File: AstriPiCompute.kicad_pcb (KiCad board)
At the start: 2 copper layers, 50.8 x 74.9 mm, 37 parts, among them J01_OUT1 12V, J02_OUT1 12V, J03_OUT1 12V, J1 Connector-ML_RPi_GPIO, Q1 TIP3055, Q2 TIP122, Q3 TIP122, U1 IRF7313, U2 MP1584EN-LF-Z

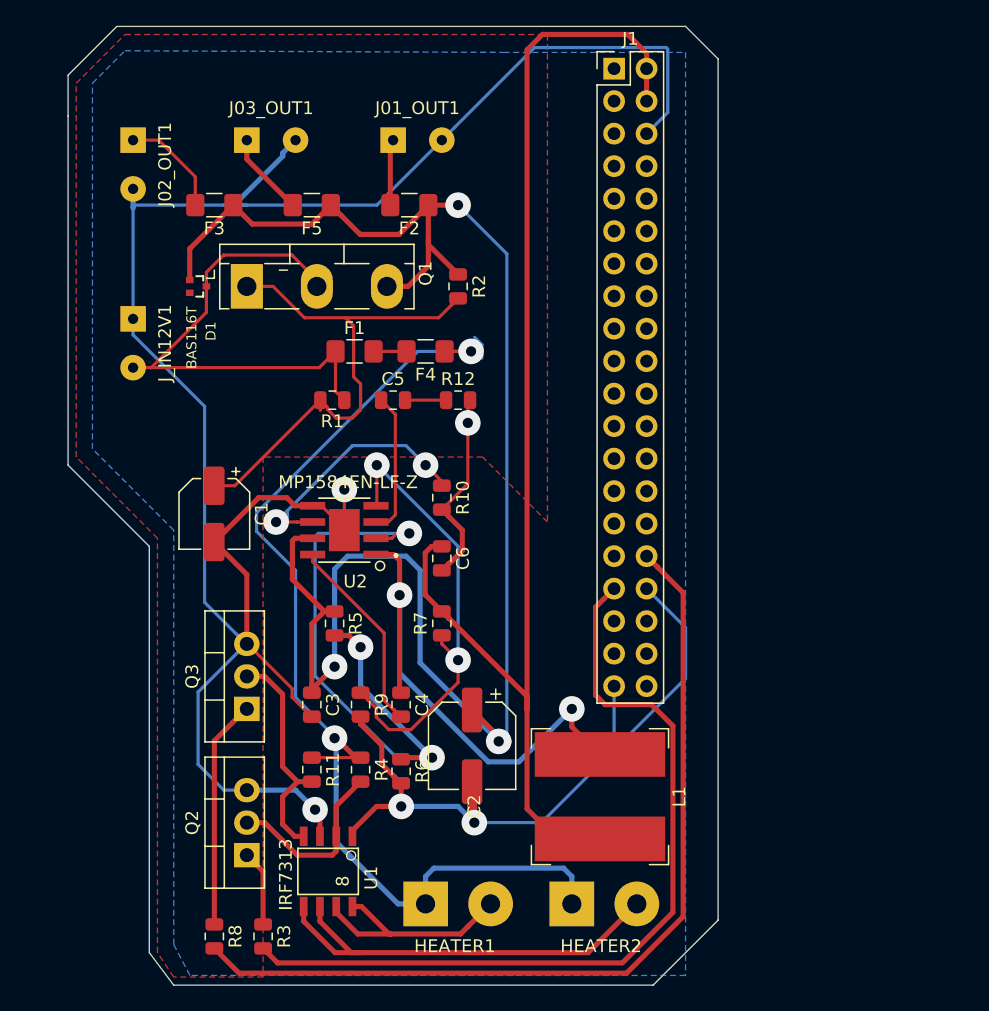
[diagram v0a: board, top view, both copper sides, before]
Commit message: Layout redesign. More compact footprint PCB
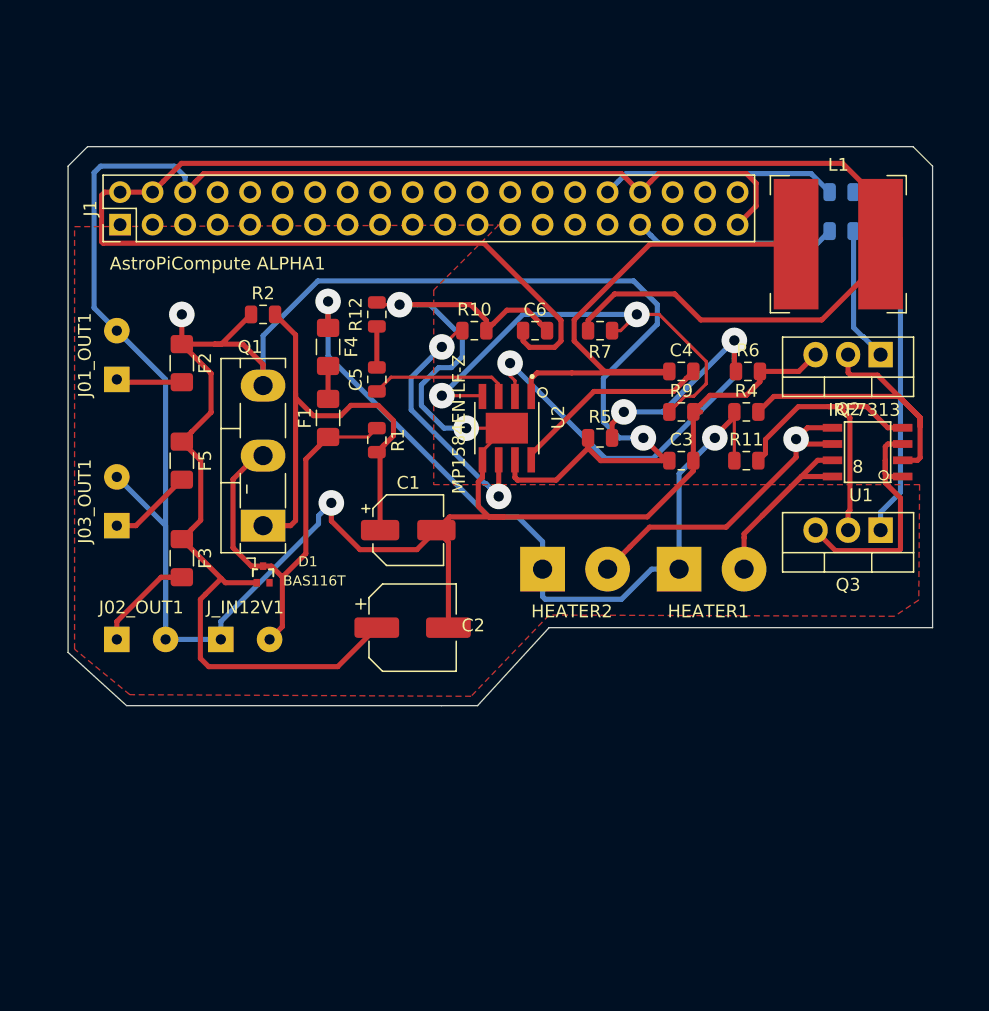
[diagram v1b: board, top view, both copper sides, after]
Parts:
- R3, R8: moved to B.Cu
- moved R8 76.1 mm to (60.5, 9.14), turned to 180 degrees
- moved R3 71.3 mm to (60.5, 12.2), turned to 180 degrees
- moved Q2 63.1 mm to (63.5, 21.8), turned to 180 degrees
- moved U1 53.4 mm to (62.5, 29.5), turned to 180 degrees
- moved Q3 51.5 mm to (63.5, 35.6), turned to 180 degrees
- moved L1 47.0 mm to (60.2, 13.2), turned to 0 degrees
- moved R11 41.7 mm to (53.0, 30.1), turned to 0 degrees
- moved R6 41.4 mm to (53.1, 23.2), turned to 0 degrees
- moved R4 41.1 mm to (53.0, 26.3), turned to 0 degrees
- moved J1 40.5 mm to (4.06, 11.7), turned to 90 degrees
- moved J02_OUT1 39.0 mm to (3.81, 44.1), turned to 0 degrees
- moved C3 34.6 mm to (47.9, 30.1), turned to 0 degrees
- moved C4 34.0 mm to (47.9, 23.2), turned to 0 degrees
- moved R9 33.9 mm to (47.9, 26.3), turned to 0 degrees
- moved HEATER1 32.8 mm to (47.8, 38.6)
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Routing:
- net GPIO_PWM01: track 68.6 -> 18.6 mm
- net GPIO_PWM02: track 64.7 -> 15.8 mm
- net +5V: track 97.3 -> 142.9 mm
- net GND: track 234.0 -> 256.5 mm, vias 5 -> 3
- net Net-(F4-Pad1): track 85.2 -> 66.4 mm
- net Net-(Q2-Pad2): track 14.4 -> 27.6 mm
- net Net-(Q3-Pad1): track 17.9 -> 28.6 mm
- net Net-(HEATER2-Pad2): track 35.1 -> 26.0 mm, vias 0 -> 1
- net Net-(Q3-Pad2): track 17.7 -> 25.2 mm
- net FLT_12V: track 139.8 -> 133.5 mm, vias 3 -> 2
- net Net-(D1-Pad3): track 40.2 -> 35.1 mm
- net Net-(Q2-Pad1): track 5.94 -> 10.6 mm
- net Net-(C1-Pad1): track 42.6 -> 38.1 mm
- net Net-(R5-Pad2): track 48.8 -> 44.7 mm
- net Net-(C4-Pad1): track 41.8 -> 43.0 mm, vias 2 -> 0
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- removed copper zone on B.Cu, net GND
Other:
- board size 50.8 x 74.9 mm -> 67.6 x 43.7 mm
- board text added: "AstroPiCompute ALPHA1"

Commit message: Beautify pcb cutout
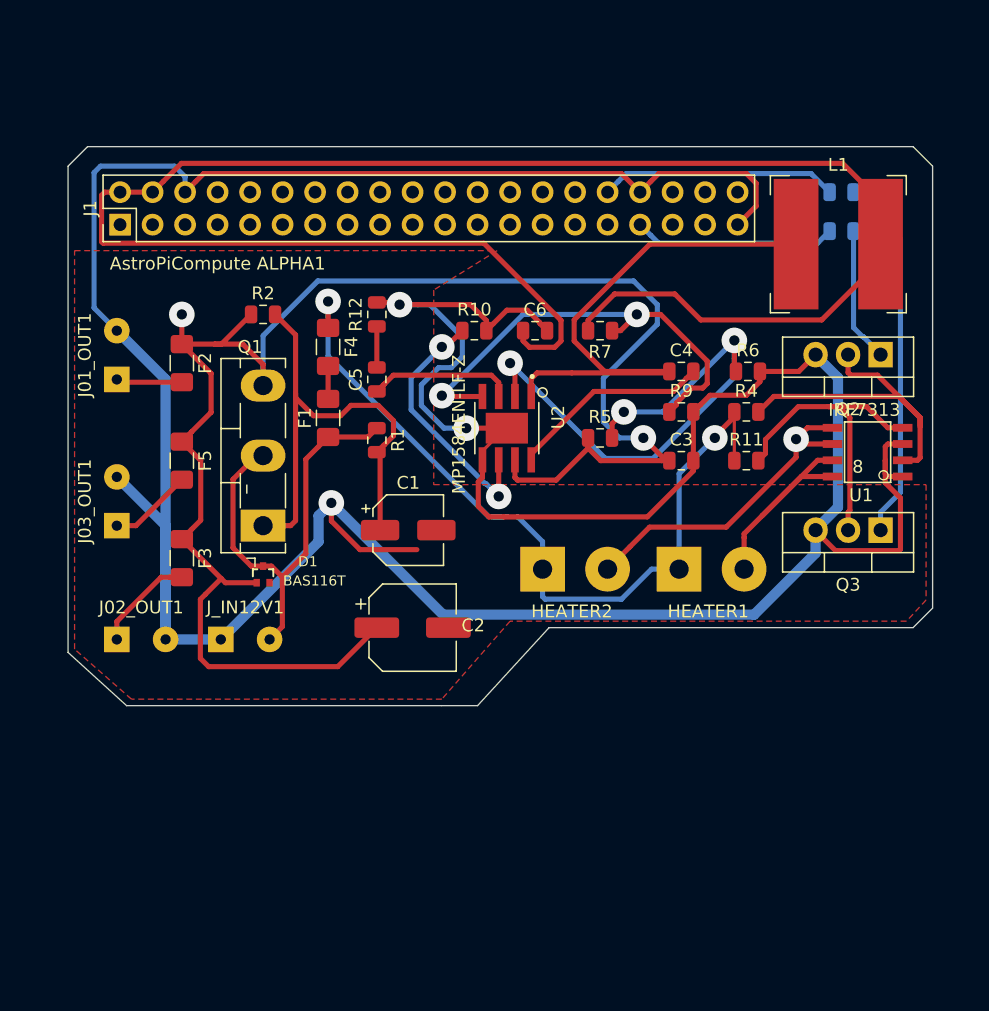
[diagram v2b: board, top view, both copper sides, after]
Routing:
- net GND: track 256.5 -> 300.7 mm
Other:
- outline, holes or cut-outs redrawn

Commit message: Minor changes. Added project mindmap with ideas
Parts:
- moved J02_OUT1 14.6 mm to (3.81, 29.5), turned to 90 degrees
- moved F3 10.0 mm to (8.89, 27.7)
- moved F5 6.16 mm to (8.89, 36.3)
- moved F2 3.17 mm to (8.89, 19.3)
- moved J03_OUT1 2.89 mm to (3.81, 38.1)
- moved J01_OUT1 2.70 mm to (3.81, 21.1)
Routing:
- net GND: track 300.7 -> 285.3 mm, vias 3 -> 2
- net FLT_12V: track 133.5 -> 140.1 mm, vias 2 -> 1
- net Net-(F4-Pad1): track 66.4 -> 69.8 mm
- net Net-(F3-Pad2): track 7.91 -> 5.19 mm
- net Net-(F2-Pad2): track 5.48 -> 7.51 mm
- net Net-(F5-Pad2): track 6.57 -> 5.22 mm

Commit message: Major PCB changes. Termal releaf areas added
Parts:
- added TP_5V1: TestPoint_Flag, TestPoint:TestPoint_Pad_1.0x1.0mm, F.Cu at (66.8, 17.7)
- added TP_GND1: TestPoint_Flag, TestPoint:TestPoint_Pad_1.0x1.0mm, F.Cu at (66.8, 19.6)
- D1: value BAS116T -> 1N4001; footprint BAS116T:SOT416 -> Diode_SMD:D_0805_2012Metric_Pad1.15x1.40mm_HandSolder
- moved D1 1.70 mm to (14.2, 40.4), turned to 180 degrees
- moved F2 1.27 mm to (7.62, 19.3)
- moved F3 1.27 mm to (7.62, 27.7)
- moved F5 1.27 mm to (7.62, 36.3)
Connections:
- D1 pad 1: FLT_12V -> Net-(D1-Pad1)
- D1 pad 2: (no net) -> FLT_12V
- F1 pad 1: Net-(D1-Pad3) -> Net-(D1-Pad1)
- J_IN12V1 pad 2: Net-(D1-Pad3) -> Net-(D1-Pad1)
- Q1 pad 2: Net-(D1-Pad3) -> Net-(D1-Pad1)
- R1 pad 1: Net-(D1-Pad3) -> Net-(D1-Pad1)
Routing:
- net GND: track 285.3 -> 342.8 mm, vias 2 -> 72
- net Net-(D1-Pad3): track 35.1 -> 0.00 mm
- net +5V: track 142.9 -> 159.6 mm
- net FLT_12V: track 140.1 -> 123.6 mm, vias 1 -> 11
- net Net-(C1-Pad1): track 38.1 -> 49.9 mm
- net Net-(D1-Pad1): track 0.00 -> 4.60 mm, vias 0 -> 20
- net Net-(F2-Pad2): track 7.51 -> 4.27 mm
- net Net-(F4-Pad1): track 69.8 -> 68.0 mm
- net Net-(F5-Pad2): track 5.22 -> 3.95 mm
- net Net-(F3-Pad2): track 5.19 -> 3.92 mm
- net Net-(HEATER1-Pad2): track 18.8 -> 17.8 mm
- added copper zone on F.Cu, net +5V
- added copper zone on B.Cu, net FLT_12V
- added copper zone on F.Cu, net FLT_12V
- added copper zone on B.Cu, net GND
- added copper zone on F.Cu, net Net-(C4-Pad1)
- added copper zone on B.Cu, net Net-(D1-Pad1)
- added copper zone on F.Cu, net Net-(D1-Pad1)
- added copper zone on F.Cu, net Net-(HEATER1-Pad2)
- added copper zone on F.Cu, net Net-(HEATER2-Pad2)

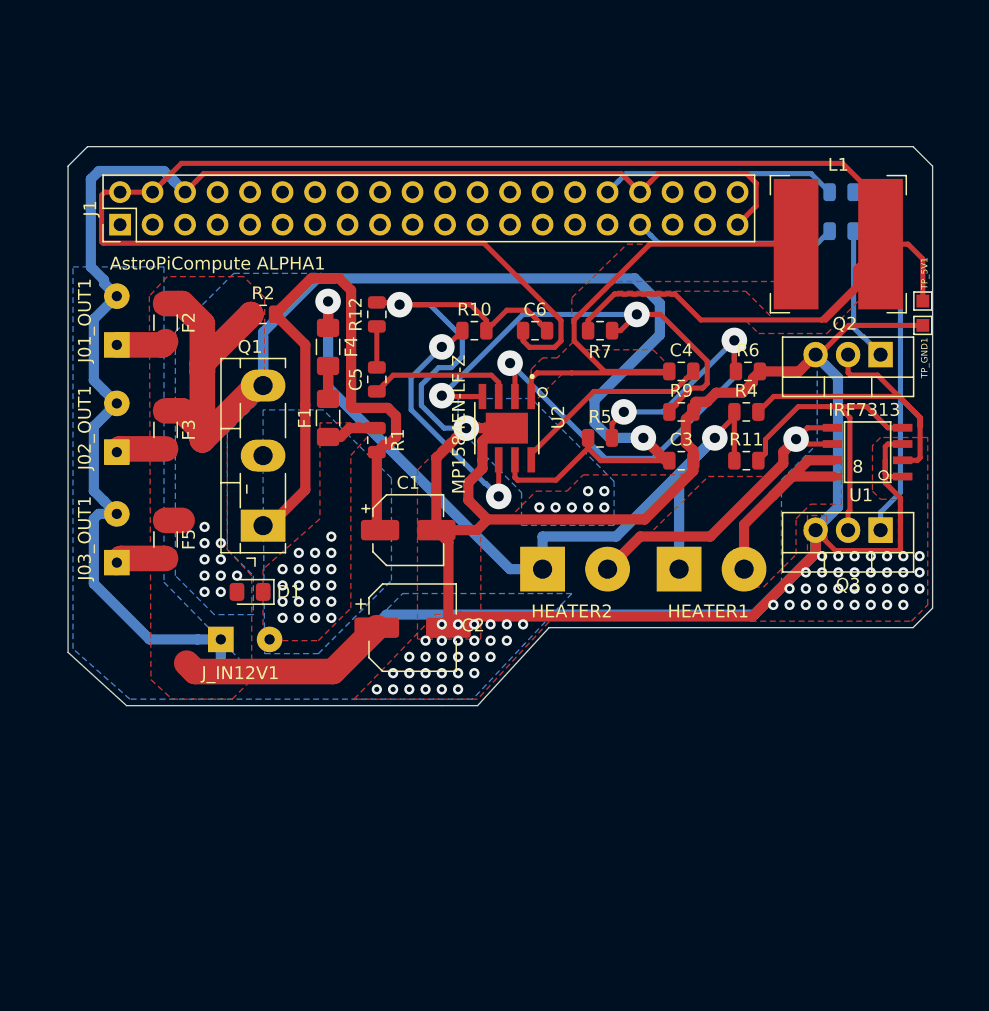
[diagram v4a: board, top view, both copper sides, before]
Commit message: Reworked 12V connectors  for 5mm size
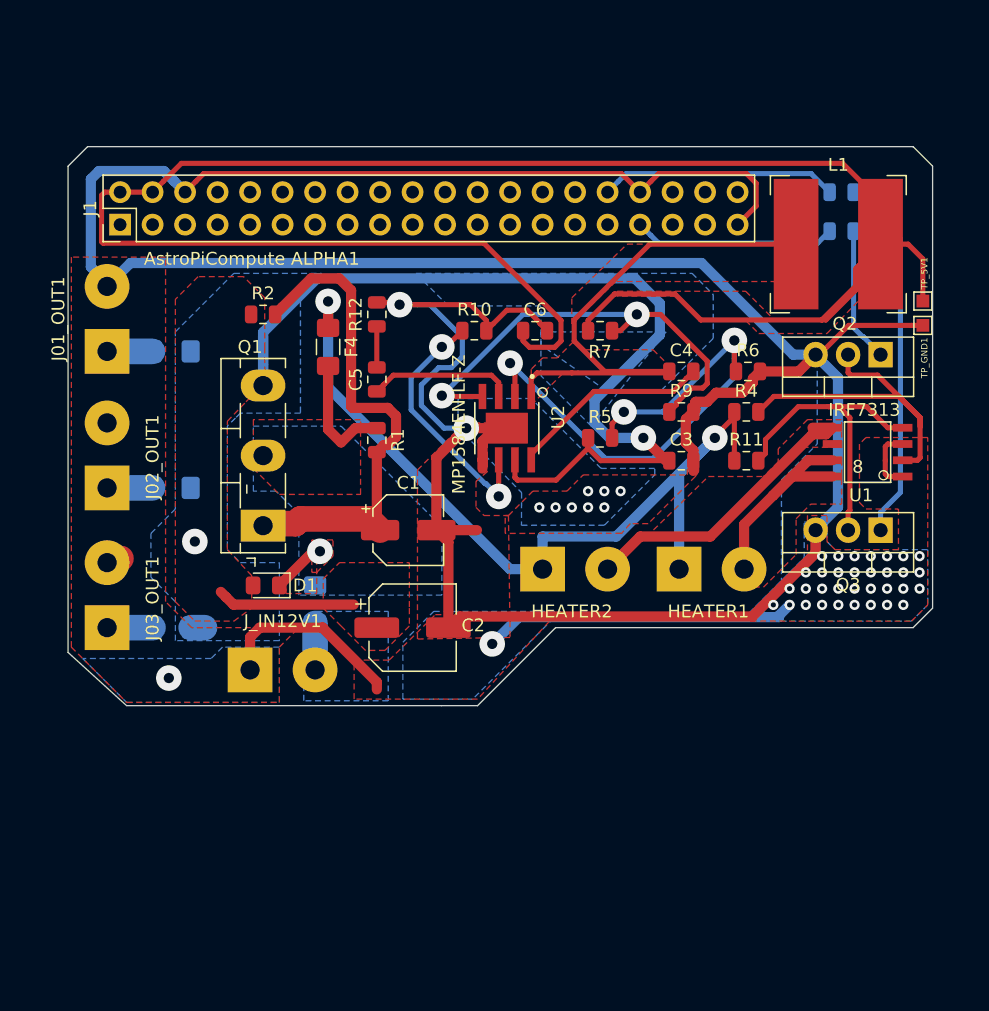
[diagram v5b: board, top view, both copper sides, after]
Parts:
- F1, F2, F3, F5: moved to B.Cu
- J01_OUT1, J02_OUT1, J03_OUT1, J_IN12V1: footprint Connector_Wire:SolderWirePad_1x02_P3.81mm_Drill0.8mm -> Connector_Wire:SolderWirePad_1x02_P5.08mm_Drill1.5mm
- moved F1 14.6 mm to (19.3, 41.4), turned to 270 degrees
- moved F5 6.91 mm to (8.13, 43.2), turned to 180 degrees
- moved J03_OUT1 5.14 mm to (3.05, 43.2)
- moved F3 4.56 mm to (8.09, 32.3), turned to 180 degrees
- moved J_IN12V1 3.30 mm to (14.2, 46.5)
- moved J02_OUT1 2.90 mm to (3.05, 32.3)
- moved F2 2.30 mm to (8.09, 21.6), turned to 180 degrees
- moved D1 1.36 mm to (15.5, 39.9)
- moved J01_OUT1 0.92 mm to (3.05, 21.6)
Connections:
- D1 pad 1: Net-(D1-Pad1) -> IN_12V
- F1 pad 1: Net-(D1-Pad1) -> IN_12V
- F1 pad 2: IN_12V -> Net-(F1-Pad2)
- J_IN12V1 pad 2: Net-(D1-Pad1) -> Net-(F1-Pad2)
- Q1 pad 2: Net-(D1-Pad1) -> IN_12V
- R1 pad 1: Net-(D1-Pad1) -> IN_12V
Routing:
- net FLT_12V: track 123.6 -> 88.2 mm, vias 11 -> 2
- net GND: track 342.8 -> 317.6 mm, vias 72 -> 45
- net IN_12V: track 2.58 -> 14.1 mm, vias 0 -> 1
- net Net-(C1-Pad1): track 49.9 -> 40.8 mm
- net Net-(D1-Pad1): track 4.60 -> 0.00 mm, vias 20 -> 0
- net Net-(F1-Pad2): track 0.00 -> 3.63 mm
- net Net-(HEATER2-Pad2): track 25.7 -> 23.7 mm, vias 1 -> 0
- added copper zone on B.Cu, net IN_12V
- added copper zone on F.Cu, net IN_12V
- added copper zone on B.Cu, net Net-(F1-Pad2)
- removed copper zone on B.Cu, net Net-(D1-Pad1)
- removed copper zone on F.Cu, net Net-(D1-Pad1)
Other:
- outline, holes or cut-outs redrawn

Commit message: Fine-tunes for milling w/ The Ant PCB
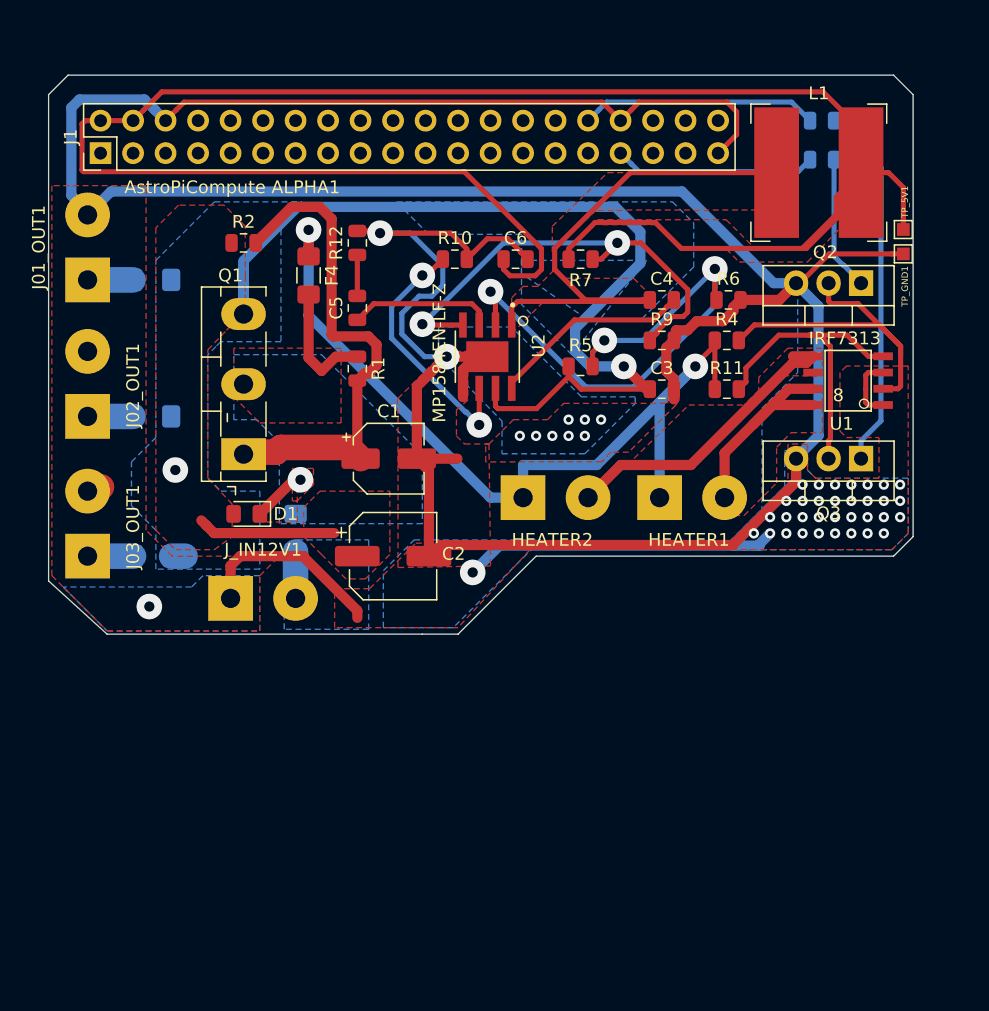
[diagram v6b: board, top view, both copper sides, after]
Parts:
- moved C1 5.79 mm to (25.1, 30.0)
- moved C2 5.79 mm to (25.4, 37.6)
- moved C5 5.79 mm to (22.6, 18.2)
- moved C6 5.79 mm to (35.0, 14.4)
- moved D1 5.79 mm to (14.0, 34.3)
- moved F2 5.79 mm to (6.57, 16.0)
- moved F3 5.79 mm to (6.57, 26.7)
- moved F4 5.79 mm to (18.8, 15.7)
- moved F5 5.79 mm to (6.60, 37.6)
- moved J01_OUT1 5.79 mm to (1.52, 16.0)
- moved J02_OUT1 5.79 mm to (1.52, 26.7)
- moved J03_OUT1 5.79 mm to (1.52, 37.6)
- moved J_IN12V1 5.79 mm to (12.7, 40.9)
- moved Q1 5.79 mm to (13.7, 29.6)
- moved Q2 5.79 mm to (62.0, 16.3)
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
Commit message: Square PCB for easy milling and testing
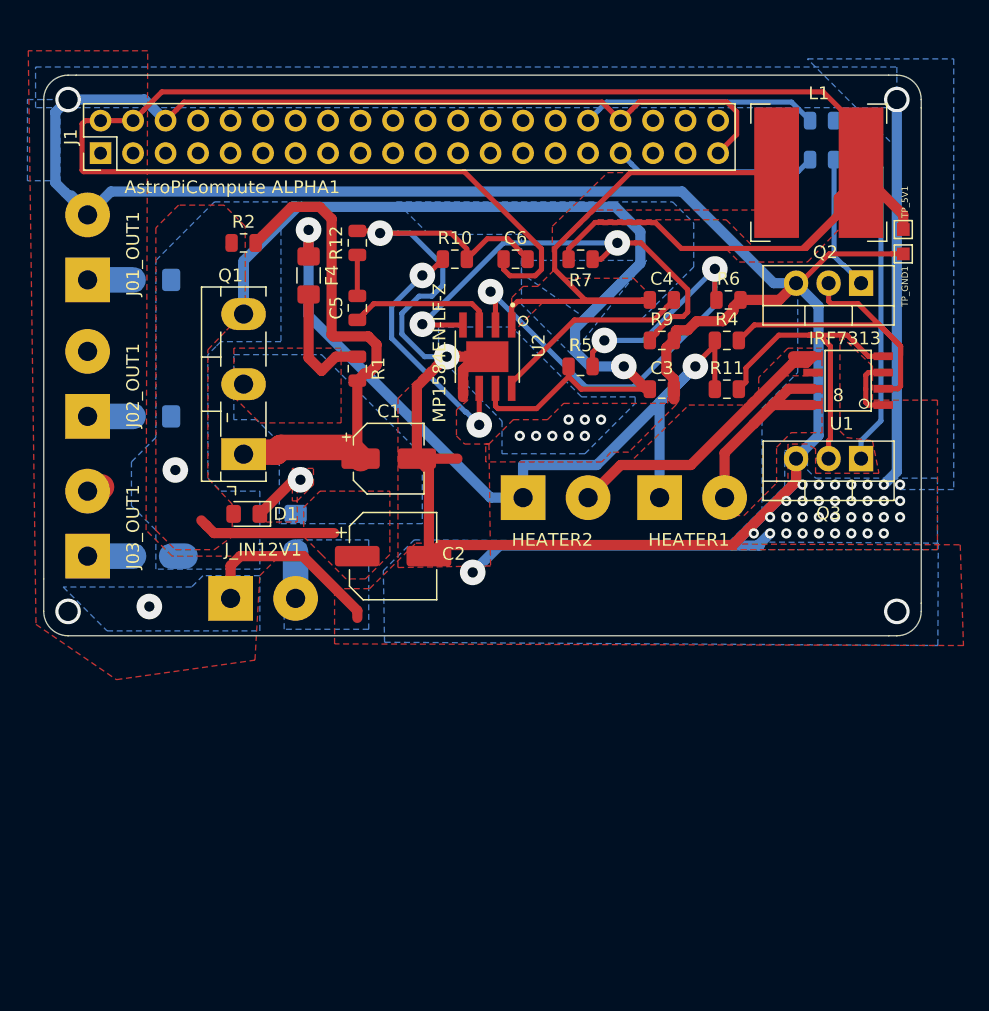
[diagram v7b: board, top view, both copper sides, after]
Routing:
- net GND: track 317.6 -> 351.7 mm, vias 45 -> 49
- net +5V: track 159.6 -> 158.3 mm
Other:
- board size 67.6 x 43.7 mm -> 68.6 x 43.8 mm
